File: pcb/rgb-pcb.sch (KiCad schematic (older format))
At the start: 35 parts, among them IC1 5V_REG, IC2 ATMEGA328P_TQFP, IC3 TLC5940, IC4 MAX3232, J1 SERIAL-POWER_out, J2 SERIAL-POWER_in, P1 AVR_ISP, P2 DEBUG, Y1 16MHz

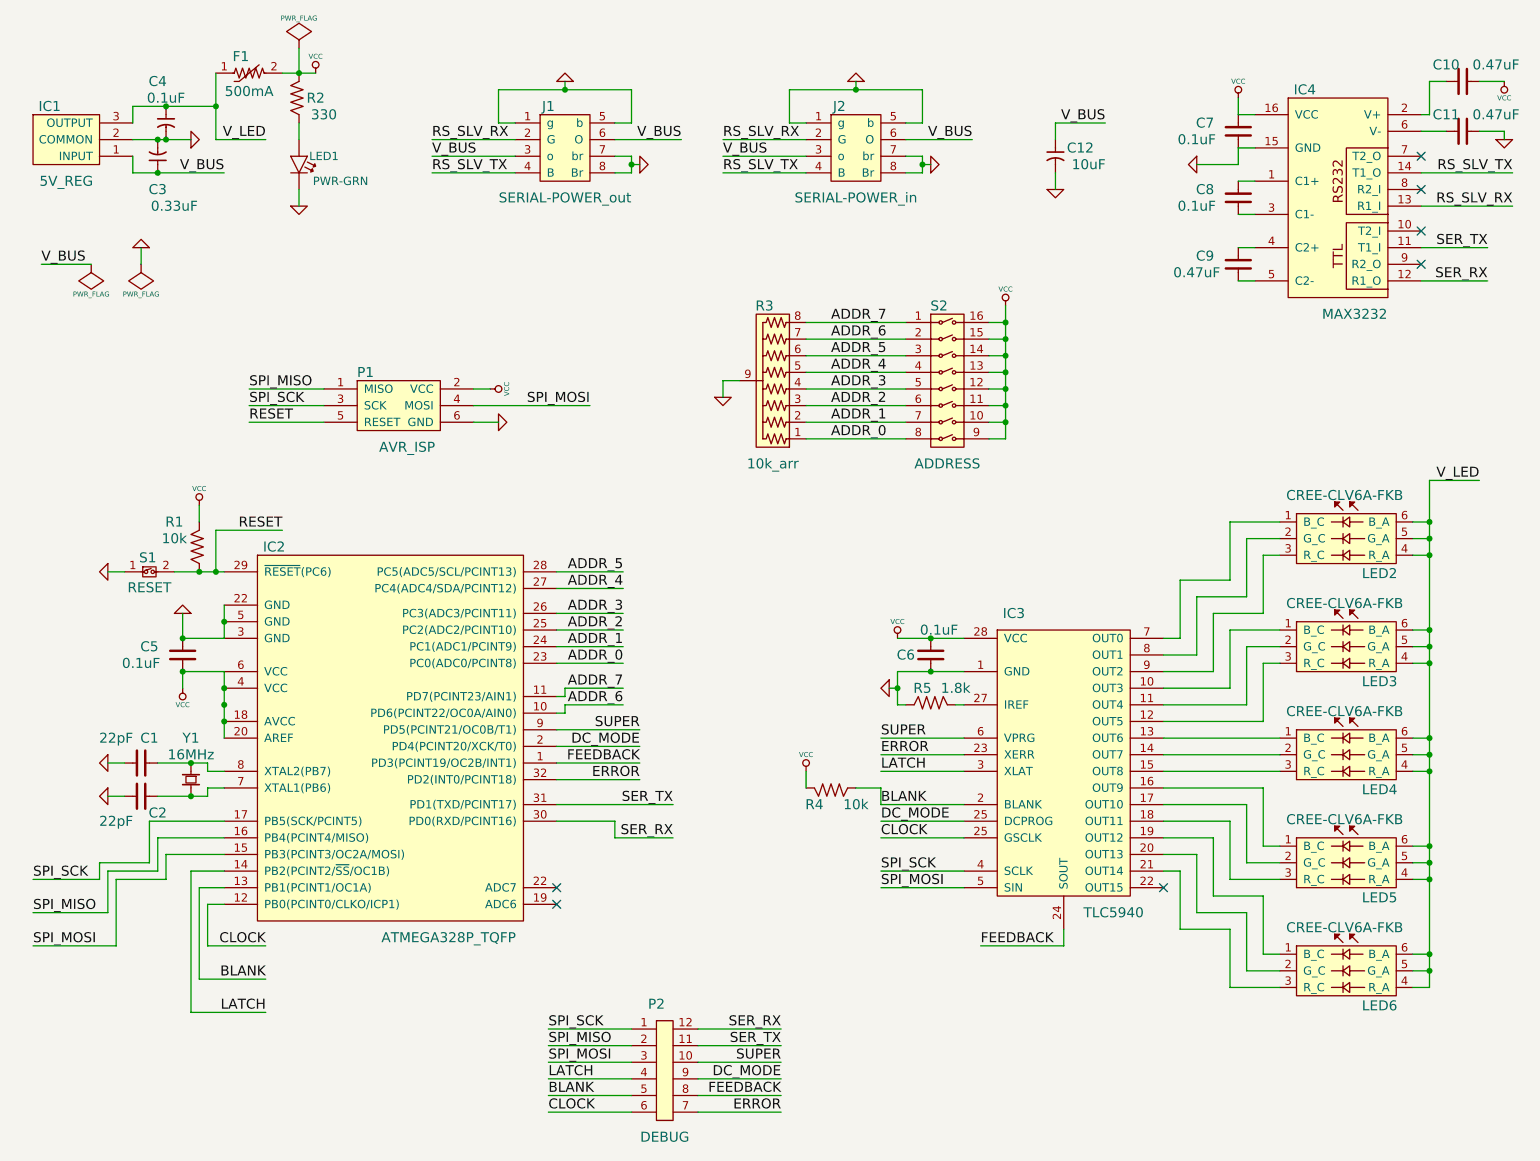
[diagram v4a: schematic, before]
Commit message: Started mapping components to footprints
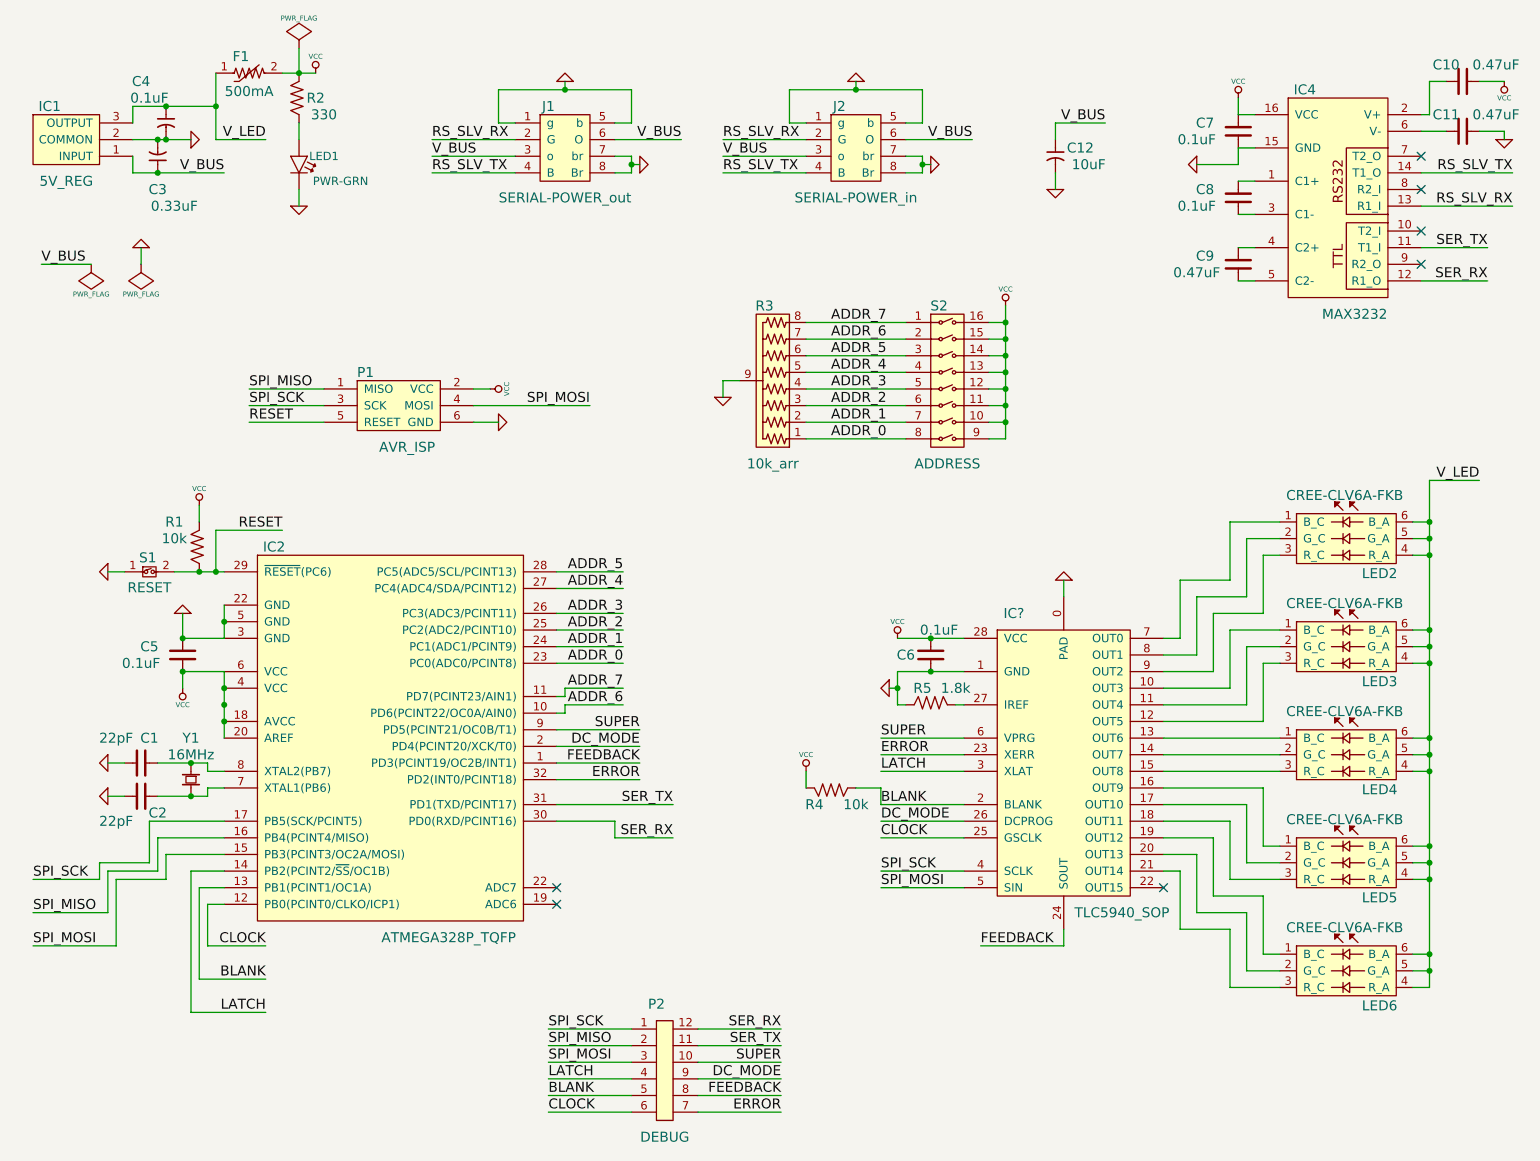
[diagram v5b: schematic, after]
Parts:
- removed IC3: TLC5940, symbol TLC5940
- added IC?: TLC5940_SOP, symbol TLC5940_SOP
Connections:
- net BLANK: now also IC?.2 (BLANK)
- net CLOCK: now also IC?.25 (GSCLK)
- net DC_MODE: now also IC?.26 (DCPROG)
- net ERROR: now also IC?.23 (XERR)
- net FEEDBACK: now also IC?.24 (SOUT)
- net GND: now also IC?.0 (PAD), IC?.1 (GND)
- net LATCH: now also IC?.3 (XLAT)
- net SPI_MOSI: now also IC?.5 (SIN)
- net SPI_SCK: now also IC?.4 (SCLK)
- net SUPER: now also IC?.6 (VPRG)
- net VCC: now also IC?.28 (VCC)
- net at LED2.1 (B_C): now also IC?.7 (OUT0)
- net at LED2.2 (G_C): now also IC?.8 (OUT1)
- net at LED2.3 (R_C): now also IC?.9 (OUT2)
- net at LED3.1 (B_C): now also IC?.10 (OUT3)
- net at LED3.2 (G_C): now also IC?.11 (OUT4)
- net at LED3.3 (R_C): now also IC?.12 (OUT5)
- net at LED4.1 (B_C): now also IC?.13 (OUT6)
- net at LED4.2 (G_C): now also IC?.14 (OUT7)
- net at LED4.3 (R_C): now also IC?.15 (OUT8)
- net at LED5.1 (B_C): now also IC?.16 (OUT9)
- net at LED5.2 (G_C): now also IC?.17 (OUT10)
- net at LED5.3 (R_C): now also IC?.18 (OUT11)
- net at LED6.1 (B_C): now also IC?.19 (OUT12)
- net at LED6.2 (G_C): now also IC?.20 (OUT13)
- net at LED6.3 (R_C): now also IC?.21 (OUT14)
- net at R5.2: now also IC?.27 (IREF)
